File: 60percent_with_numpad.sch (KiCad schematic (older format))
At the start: 176 parts

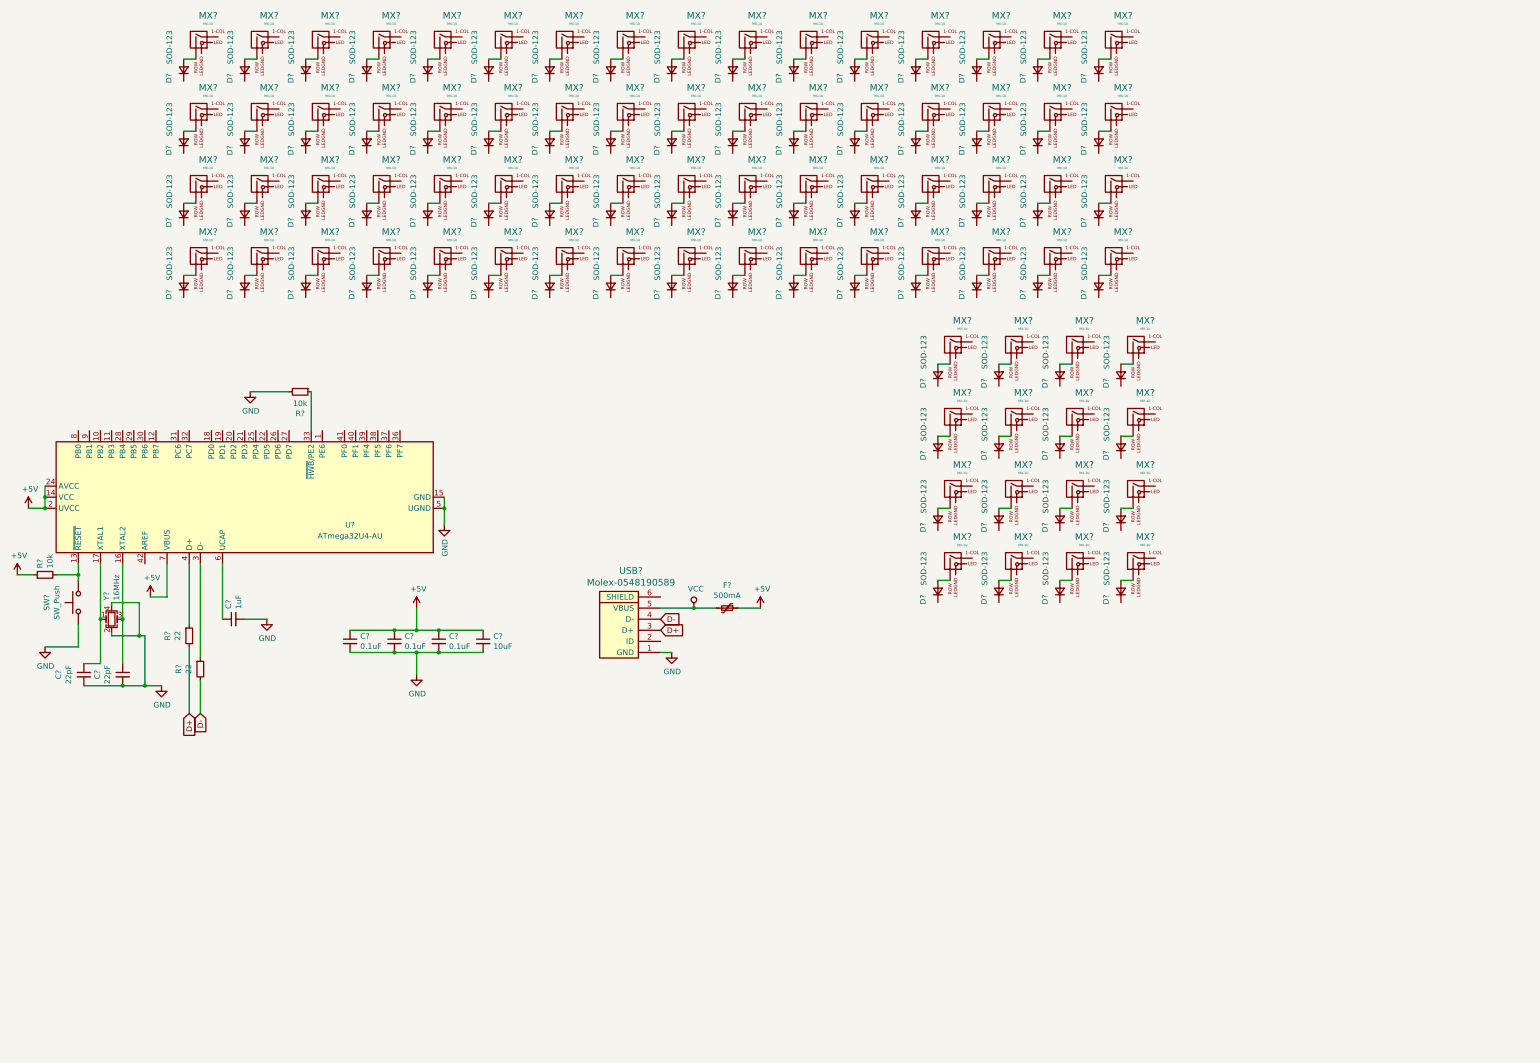
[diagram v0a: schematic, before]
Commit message: split into h-sheets
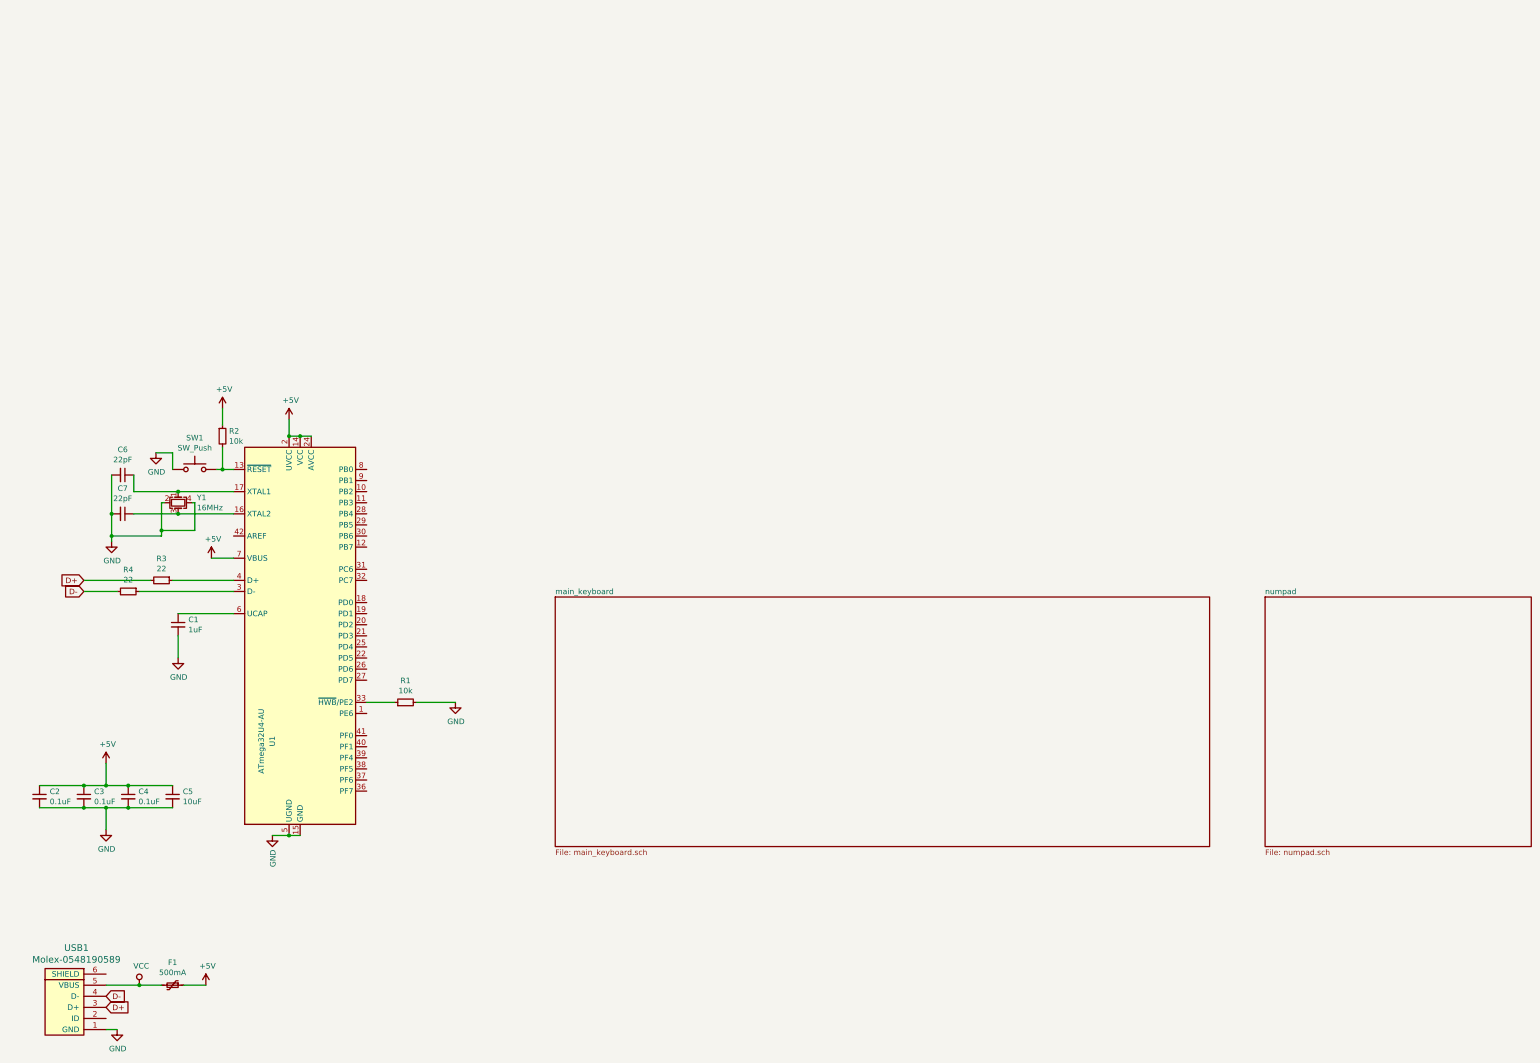
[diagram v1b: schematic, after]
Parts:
- removed D? (x80): SOD-123, symbol Device:D_Small
- removed MX? (x80): MX-1U, symbol MX_Alps_Hybrids:MX-1U
- C1, C2, C3, C4, C5, C6: renamed from C?; footprint (none) -> Capacitors_SMD:C_0805
- C7: renamed from C?; footprint (none) -> Diodes_SMD:D_SOD-123
- F1: renamed from F?; footprint (none) -> MX_Alps_Hybrid:MX-1U
- R1, R2, R3, R4: renamed from R?; footprint (none) -> Resistors_SMD:R_0805
- SW1: renamed from SW?; footprint (none) -> random-keyboard-parts:SKQG-1155865
- U1: renamed from U?; footprint Package_QFP:TQFP-44_10x10mm_P0.8mm -> Housings_QFP:TQFP-44_10x10mm_Pitch0.8mm
- USB1: renamed from USB?; footprint (none) -> random-keyboard-parts:Molex-0548190589
- Y1: renamed from Y?; footprint (none) -> Crystals:Crystal_SMD_3225-4pin_3.2x2.5mm
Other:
- moved on the sheet: C1, C2, C3, C4, C5, C6, C7, F1, R1, R2, R3, R4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
